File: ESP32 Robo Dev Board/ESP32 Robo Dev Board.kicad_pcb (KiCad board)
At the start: 2 copper layers, 61.3 x 61.3 mm, 59 parts, among them U1 ESP32-S3-WROOM-1, U102 AMS1117-3.3, U201 STSPIN250, U301 STSPIN250

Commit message: First Finished Version 0.1.
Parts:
- added J1: PRG, Connector:Tag-Connect_TC2050-IDC-FP_2x05_P1.27mm_Vertical, F.Cu at (156.3, 75.8)
- moved Rr1 14.3 mm to (134.5, 94.8), turned to 180 degrees
- moved J_B1 3.06 mm to (152.4, 79.2)
- moved E1 1.06 mm to (161.8, 86.5)
- moved Cr1 0.32 mm to (134.4, 92.8)
- renumbered C101 to C1, C102 to C2, C201 to C3, C202 to C4, C301 to C5, C302 to C6, Cen101 to Cen1, Coff201 to Coff1, Coff301 to Coff2, C_ref201 to Cr1, C_ref301 to Cr2, Cs101 to Cs1, D101 to D1, D102 to D2, E101 to E1, E102 to E2, J_A101 to J_A1, J_B101 to J_B1, R101 to R1, R408 to R10, R409 to R11, R410 to R12, R411 to R13, R412 to R14, R413 to R15, R414 to R16, R415 to R17, R416 to R18, R102 to R2, R401 to R3, R402 to R4, R403 to R5, R404 to R6, R405 to R7, R406 to R8, R407 to R9, Ren101 to Ren1, Roff201 to Roff1, Roff202 to Roff2, Roff301 to Roff3, Roff302 to Roff4, R_ref201 to Rr1, R_ref301 to Rr2, Rs101 to Rs1, Rsns201 to Rsns1, Rsns301 to Rsns2, S401 to S1, S402 to S2, S403 to S3, S404 to S4, S405 to S5, S406 to S6, S407 to S7, S408 to S8, U102 to U2, U201 to U3, U301 to U4
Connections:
- U1 pad 27: unconnected-(U1-Pad27) -> /Boot
- U1 pad 3: unconnected-(U1-Pad3) -> /Enable
- U1 pad 31: unconnected-(U1-Pad31) -> /L_Signal_A
- U1 pad 32: unconnected-(U1-Pad32) -> /L_Signal_B
- U1 pad 33: unconnected-(U1-Pad33) -> /R_Signal_B
- U1 pad 34: unconnected-(U1-Pad34) -> /R_Signal_A
- U1 pad 36: unconnected-(U1-Pad36) -> /Rx
- U1 pad 37: unconnected-(U1-Pad37) -> /Tx
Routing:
- net /IR7: track 3.31 -> 71.2 mm, vias 0 -> 1
- net /R_Signal_B: track 0.00 -> 49.8 mm, vias 0 -> 1
- net /R_Signal_A: track 0.00 -> 48.7 mm, vias 0 -> 1
- net /IR1: track 3.29 -> 51.1 mm, vias 0 -> 2
- net /PWM A: track 8.76 -> 50.9 mm, vias 0 -> 2
- net /IR8: track 2.94 -> 45.0 mm, vias 0 -> 1
- net /IR2: track 3.06 -> 42.9 mm, vias 0 -> 2
- net /Enable: track 0.00 -> 37.2 mm, vias 0 -> 2
- net +3V3: track 249.6 -> 284.3 mm, vias 2 -> 6
- net /IR6: track 3.09 -> 35.8 mm, vias 0 -> 2
- net /IR4: track 3.04 -> 34.5 mm, vias 0 -> 2
- net /IR5: track 3.45 -> 32.8 mm, vias 0 -> 2
- net /IR3: track 2.81 -> 30.1 mm, vias 0 -> 2
- net /Boot: track 0.00 -> 24.1 mm, vias 0 -> 2
- net GND: track 25.7 -> 40.4 mm, vias 11 -> 27
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
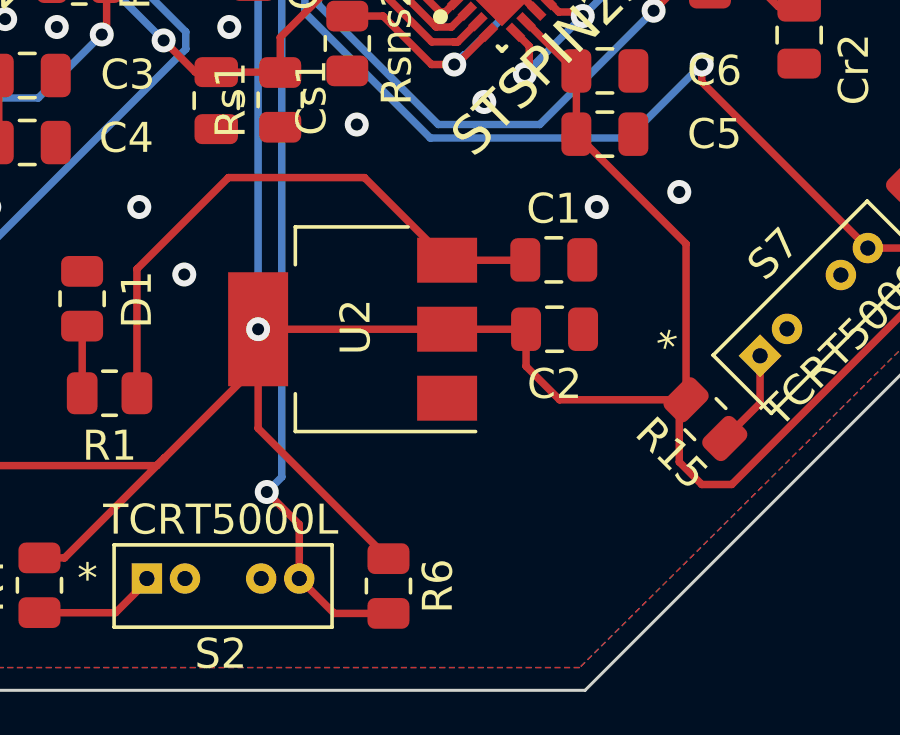
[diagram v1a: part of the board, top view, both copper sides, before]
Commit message: Add battery connector
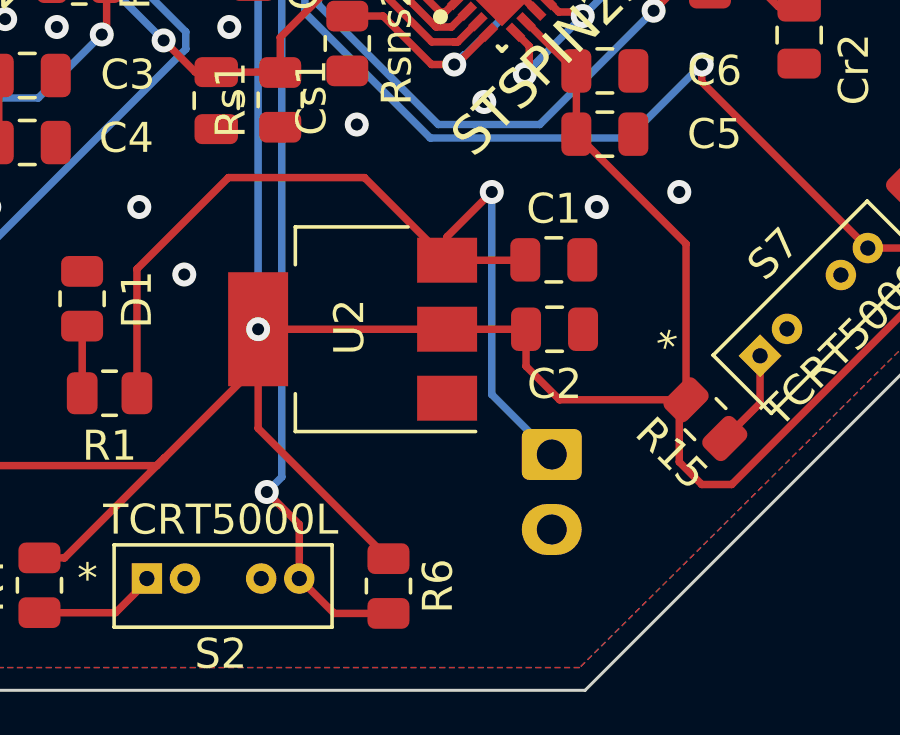
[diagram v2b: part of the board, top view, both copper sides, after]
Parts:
- added J_B2: Batt In, Connector_JST:JST_EH_B2B-EH-A_1x02_P2.50mm_Vertical, B.Cu at (150.2, 110.5)
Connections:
- net +5V renamed Net-(C1-Pad1)
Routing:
- net Net-(C1-Pad1): track 19.5 -> 32.0 mm, vias 0 -> 1
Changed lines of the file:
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@@
   )
   (net 0 "")
-  (net 1 "+5V")
+  (net 1 "Net-(C1-Pad1)")
   (net 2 "GND")
   (net 3 "+3V3")
@@
     (fp_line (start 1 0.625) (end -1 0.625) (layer "F.Fab") (width 0.1))
     (pad "1" smd roundrect (at -0.95 0) (size 1 1.45) (layers "F.Cu" "F.Paste" "F.Mask") (roundrect_rratio 0.25)
-      (net 1 "+5V") (pintype "passive"))
+      (net 1 "Net-(C1-Pad1)") (pintype "passive"))
     (pad "2" smd roundrect (at 0.95 0) (size 1 1.45) (layers "F.Cu" "F.Paste" "F.Mask") (roundrect_rratio 0.25)
       (net 2 "GND") (pintype "passive"))
@@
     (property "Sheetname" "")
     (attr smd)
-    (fp_text reference "U2" (at -0.1016 0.0762 90) (layer "F.SilkS")
+    (fp_text reference "U2" (at 0.1116 0.0744 90) (layer "F.SilkS")
       (effects (font (size 1 1) (thickness 0.15)))
     )
@@
       (net 3 "+3V3") (pinfunction "VO") (pintype "power_out"))
     (pad "3" smd rect (at -3.15 2.3 180) (size 2 1.5) (layers "F.Cu" "F.Paste" "F.Mask")
-      (net 1 "+5V") (pinfunction "VI") (pintype "power_in"))
+      (net 1 "Net-(C1-Pad1)") (pinfunction "VI") (pintype "power_in"))
     (model "${KICAD6_3DMODEL_DIR}/Package_TO_SOT_SMD.3dshapes/SOT-223.wrl"
       (offset (xyz 0 0 0))
@@
       (net 14 "Net-(D1-Pad2)") (pintype "passive"))
     (pad "2" smd roundrect (at 0.9125 0) (size 1.025 1.4) (layers "F.Cu" "F.Paste" "F.Mask") (roundrect_rratio 0.243902)
-      (net 1 "+5V") (pintype "passive"))
+      (net 1 "Net-(C1-Pad1)") (pintype "passive"))
     (model "${KICAD6_3DMODEL_DIR}/Resistor_SMD.3dshapes/R_0805_2012Metric.wrl"
       (offset (xyz 0 0 0))
@@
     )
   )
+  (footprint "Connector_JST:JST_EH_B2B-EH-A_1x02_P2.50mm_Vertical" (layer "B.Cu")
+    (at 150.25 110.5 -90)
+    (descr "JST EH series connector, B2B-EH-A (http://www.jst-mfg.com/product/pdf/eng/eEH.pdf), generated with kicad-footprint-generator")
+    (tags "connector JST EH vertical")
+    (property "Sheetfile" "ESP32 Robo Dev Board.kicad_sch")
+    (property "Sheetname" "")
+    (attr through_hole)
+    (fp_text reference "J_B2" (at 1.25 2.8 90) (layer "B.SilkS")
+      (effects (font (size 1 1) (thickness 0.15)) (justify mirror))
+    )
+    (fp_text value "Batt In" (at 1.25 -3.4 90) (layer "B.Fab")
+      (effects (font (size 1 1) (thickness 0.15)) (justify mirror))
+    )
+    (fp_text user "${REFERENCE}" (at 1.25 -1.5 90) (layer "B.Fab")
+      (effects (font (size 1 1) (thickness 0.15)) (justify mirror))
+    )
+    (fp_line (start -2.91 -2.61) (end -0.41 -2.61) (layer "B.SilkS") (width 0.12))
+    (fp_line (start 5.11 1.71) (end -2.61 1.71) (layer "B.SilkS") (width 0.12))
+    (fp_line (start -1.61 -0.81) (end -1.61 -2.31) (layer "B.SilkS") (width 0.12))
+    (fp_line (start -2.61 -2.31) (end 5.11 -2.31) (layer "B.SilkS") (width 0.12))
+    (fp_line (start 5.11 -0.81) (end 4.11 -0.81) (layer "B.SilkS") (width 0.12))
+    (fp_line (start -2.61 0) (end -2.11 0) (layer "B.SilkS") (width 0.12))
+    (fp_line (start -2.91 -0.11) (end -2.91 -2.61) (layer "B.SilkS") (width 0.12))
+    (fp_line (start -2.61 1.71) (end -2.61 -2.31) (layer "B.SilkS") (width 0.12))
+    (fp_line (start 4.11 -0.81) (end 4.11 -2.31) (layer "B.SilkS") (width 0.12))
+    (fp_line (start -2.11 1.21) (end 4.61 1.21) (layer "B.SilkS") (width 0.12))
+    (fp_line (start 4.61 1.21) (end 4.61 0) (layer "B.SilkS") (width 0.12))
+    (fp_line (start 5.11 -2.31) (end 5.11 1.71) (layer "B.SilkS") (width 0.12))
+    (fp_line (start 4.61 0) (end 5.11 0) (layer "B.SilkS") (width 0.12))
+    (fp_line (start -2.61 -0.81) (end -1.61 -0.81) (layer "B.SilkS") (width 0.12))
+    (fp_line (start -2.11 0) (end -2.11 1.21) (layer "B.SilkS") (width 0.12))
+    (fp_line (start -3 2.1) (end -3 -2.7) (layer "B.CrtYd") (width 0.05))
+    (fp_line (start 5.5 2.1) (end -3 2.1) (layer "B.CrtYd") (width 0.05))
+    (fp_line (start 5.5 -2.7) (end 5.5 2.1) (layer "B.CrtYd") (width 0.05))
+    (fp_line (start -3 -2.7) (end 5.5 -2.7) (layer "B.CrtYd") (width 0.05))
+    (fp_line (start 5 -2.2) (end 5 1.6) (layer "B.Fab") (width 0.1))
+    (fp_line (start -2.5 1.6) (end -2.5 -2.2) (layer "B.Fab") (width 0.1))
+    (fp_line (start 5 1.6) (end -2.5 1.6) (layer "B.Fab") (width 0.1))
+    (fp_line (start -2.91 -0.11) (end -2.91 -2.61) (layer "B.Fab") (width 0.1))
+    (fp_line (start -2.91 -2.61) (end -0.41 -2.61) (layer "B.Fab") (width 0.1))
+    (fp_line (start -2.5 -2.2) (end 5 -2.2) (layer "B.Fab") (width 0.1))
+    (pad "1" thru_hole roundrect (at 0 0 270) (size 1.7 2) (drill 1) (layers *.Cu *.Mask) (roundrect_rratio 0.147059)
+      (net 1 "Net-(C1-Pad1)") (pinfunction "Pin_1") (pintype "passive"))
+    (pad "2" thru_hole oval (at 2.5 0 270) (size 1.7 2) (drill 1) (layers *.Cu *.Mask)
+      (net 2 "GND") (pinfunction "Pin_2") (pintype "passive"))
+    (model "${KICAD6_3DMODEL_DIR}/Connector_JST.3dshapes/JST_EH_B2B-EH-A_1x02_P2.50mm_Vertical.wrl"
+      (offset (xyz 0 0 0))
+      (scale (xyz 1 1 1))
+      (rotate (xyz 0 0 0))
+    )
+  )
   (footprint "Amoskeag_KiCAD_Lib:Kailh Encoder 9mm" (layer "B.Cu")
     (at 161.75 86.5 90)
@@
   (segment (start 136.4215 104.3197) (end 139.4714 101.2698) (width 0.25) (layer "F.Cu") (net 1))
   (segment (start 144.007 101.2698) (end 146.7616 104.0244) (width 0.25) (layer "F.Cu") (net 1))
+  (segment (start 148.25 101.75) (end 146.7616 103.2384) (width 0.25) (layer "F.Cu") (net 1))
   (segment (start 149.3672 104.013) (end 149.3558 104.0244) (width 0.25) (layer "F.Cu") (net 1))
+  (segment (start 146.7616 103.2384) (end 146.7616 104.0244) (width 0.25) (layer "F.Cu") (net 1))
   (segment (start 149.3558 104.0244) (end 146.7616 104.0244) (width 0.25) (layer "F.Cu") (net 1))
   (segment (start 136.4215 108.458) (end 136.4215 104.3197) (width 0.25) (layer "F.Cu") (net 1))
   (segment (start 139.4714 101.2698) (end 144.007 101.2698) (width 0.25) (layer "F.Cu") (net 1))
+  (via (at 148.25 101.75) (size 0.8) (drill 0.4) (layers "F.Cu" "B.Cu") (net 1))
+  (segment (start 148.25 108.5) (end 148.25 101.75) (width 0.25) (layer "B.Cu") (net 1))
+  (segment (start 150.25 110.5) (end 148.25 108.5) (width 0.25) (layer "B.Cu") (net 1))
   (segment (start 147.43388 94.117234) (end 148.236446 94.9198) (width 0.25) (layer "F.Cu") (net 2))
   (segment (start 157.75 73) (end 159 73) (width 0.25) (layer "F.Cu") (net 2))
